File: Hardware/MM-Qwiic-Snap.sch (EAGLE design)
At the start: 37 parts, among them J15 MICROMOD-2222-C, J2 QWIIC_RIGHT_ANGLE, U5 AP7361C-33FGEUDFN-8

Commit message: Preliminary schematic done?
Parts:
- added C3, C4: 4.7uF, SparkFun-Capacitors:4.7UF-0603-35V-(20%)
- added D3: 3A/10V/280mV, SparkFun-DiscreteSemi:DIODE-SCHOTTKY-BAT60A
- added D4: Yellow, SparkFun-LED:LED-YELLOW0603
- added JP1: JUMPER-SMT_2_NC_TRACE_SILK, SparkFun-Jumpers:JUMPER-SMT_2_NC_TRACE_SILK
- added R1: 2.2k, SparkFun-Resistors:2.2KOHM-0603-1/10W-1%
- added R4: 1k, SparkFun-Resistors:1KOHM-0603-1/10W-1%
- added U1: MCP73831, SparkFun-IC-Power:MCP73831
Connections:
- new net 5V: C4.1, D3.C, D4.A, JP1.2, U1.VIN
- new net N$2: R1.2, U1.PROG
- new net N$3: R4.1, U1.STAT
- new net N$5: C3.1, D3.A, J3.+, U1.VBAT
- new net N$8: D4.C, R4.2
- net GND: now also C3.2, C4.2, J3.-, R1.1, U1.VSS
- net VIN: now also JP1.1
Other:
- moved on the sheet: J3

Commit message: Board layout
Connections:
- net 3.3V_EN: now also J15.3.3V_EN
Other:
- note added: "Battery Charger"
- note added: "Buttons"
- note added: "Qwiic Connector"
- note added: "USB-C"
- note removed: "USB"
- moved on the sheet: BYP, C1, C10, C11, C13, C2, C3, C4, C9, D1, D2, D3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

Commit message: Layout
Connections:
- net VIN: now also J15.USB_VIN
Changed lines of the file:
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@@
 <grid distance="0.1" unitdist="inch" unit="inch" style="lines" multiple="1" display="no" altdistance="0.01" altunitdist="inch" altunit="inch"/>
 <layers>
-<layer number="1" name="Top" color="4" fill="1" visible="yes" active="no"/>
-<layer number="2" name="Route2" color="1" fill="3" visible="yes" active="no"/>
-<layer number="3" name="Route3" color="4" fill="3" visible="yes" active="no"/>
-<layer number="4" name="Route4" color="1" fill="4" visible="yes" active="no"/>
-<layer number="5" name="Route5" color="4" fill="4" visible="yes" active="no"/>
-<layer number="6" name="Route6" color="1" fill="8" visible="yes" active="no"/>
-<layer number="7" name="Route7" color="4" fill="8" visible="yes" active="no"/>
-<layer number="8" name="Route8" color="1" fill="2" visible="yes" active="no"/>
-<layer number="9" name="Route9" color="4" fill="2" visible="yes" active="no"/>
-<layer number="10" name="Route10" color="1" fill="7" visible="yes" active="no"/>
-<layer number="11" name="Route11" color="4" fill="7" visible="yes" active="no"/>
-<layer number="12" name="Route12" color="1" fill="5" visible="yes" active="no"/>
-<layer number="13" name="Route13" color="4" fill="5" visible="yes" active="no"/>
-<layer number="14" name="Route14" color="1" fill="6" visible="yes" active="no"/>
-<layer number="15" name="Route15" color="4" fill="6" visible="yes" active="no"/>
-<layer number="16" name="Bottom" color="1" fill="1" visible="yes" active="no"/>
-<layer number="17" name="Pads" color="2" fill="1" visible="yes" active="no"/>
-<layer number="18" name="Vias" color="2" fill="1" visible="yes" active="no"/>
-<layer number="19" name="Unrouted" color="6" fill="1" visible="yes" active="no"/>
-<layer number="20" name="Dimension" color="24" fill="1" visible="yes" active="no"/>
-<layer number="21" name="tPlace" color="16" fill="1" visible="yes" active="no"/>
-<layer number="22" name="bPlace" color="14" fill="1" visible="yes" active="no"/>
-<layer number="23" name="tOrigins" color="15" fill="1" visible="yes" active="no"/>
-<layer number="24" name="bOrigins" color="15" fill="1" visible="yes" active="no"/>
-<layer number="25" name="tNames" color="7" fill="1" visible="yes" active="no"/>
-<layer number="26" name="bNames" color="7" fill="1" visible="yes" active="no"/>
-<layer number="27" name="tValues" color="7" fill="1" visible="yes" active="no"/>
-<layer number="28" name="bValues" color="7" fill="1" visible="yes" active="no"/>
+<layer number="1" name="Top" color="4" fill="1" visible="no" active="no"/>
+<layer number="2" name="Route2" color="1" fill="3" visible="no" active="no"/>
+<layer number="3" name="Route3" color="4" fill="3" visible="no" active="no"/>
+<layer number="4" name="Route4" color="1" fill="4" visible="no" active="no"/>
+<layer number="5" name="Route5" color="4" fill="4" visible="no" active="no"/>
+<layer number="6" name="Route6" color="1" fill="8" visible="no" active="no"/>
+<layer number="7" name="Route7" color="4" fill="8" visible="no" active="no"/>
+<layer number="8" name="Route8" color="1" fill="2" visible="no" active="no"/>
+<layer number="9" name="Route9" color="4" fill="2" visible="no" active="no"/>
+<layer number="10" name="Route10" color="1" fill="7" visible="no" active="no"/>
+<layer number="11" name="Route11" color="4" fill="7" visible="no" active="no"/>
+<layer number="12" name="Route12" color="1" fill="5" visible="no" active="no"/>
+<layer number="13" name="Route13" color="4" fill="5" visible="no" active="no"/>
+<layer number="14" name="Route14" color="1" fill="6" visible="no" active="no"/>
+<layer number="15" name="Route15" color="4" fill="6" visible="no" active="no"/>
+<layer number="16" name="Bottom" color="1" fill="1" visible="no" active="no"/>
+<layer number="17" name="Pads" color="2" fill="1" visible="no" active="no"/>
+<layer number="18" name="Vias" color="2" fill="1" visible="no" active="no"/>
+<layer number="19" name="Unrouted" color="6" fill="1" visible="no" active="no"/>
+<layer number="20" name="Dimension" color="24" fill="1" visible="no" active="no"/>
+<layer number="21" name="tPlace" color="16" fill="1" visible="no" active="no"/>
+<layer number="22" name="bPlace" color="14" fill="1" visible="no" active="no"/>
+<layer number="23" name="tOrigins" color="15" fill="1" visible="no" active="no"/>
+<layer number="24" name="bOrigins" color="15" fill="1" visible="no" active="no"/>
+<layer number="25" name="tNames" color="7" fill="1" visible="no" active="no"/>
+<layer number="26" name="bNames" color="7" fill="1" visible="no" active="no"/>
+<layer number="27" name="tValues" color="7" fill="1" visible="no" active="no"/>
+<layer number="28" name="bValues" color="7" fill="1" visible="no" active="no"/>
 <layer number="29" name="tStop" color="7" fill="3" visible="no" active="no"/>
 <layer number="30" name="bStop" color="7" fill="6" visible="no" active="no"/>
@@
 <layer number="35" name="tGlue" color="7" fill="4" visible="no" active="no"/>
 <layer number="36" name="bGlue" color="7" fill="5" visible="no" active="no"/>
-<layer number="37" name="tTest" color="7" fill="1" visible="yes" active="no"/>
-<layer number="38" name="bTest" color="7" fill="1" visible="yes" active="no"/>
+<layer number="37" name="tTest" color="7" fill="1" visible="no" active="no"/>
+<layer number="38" name="bTest" color="7" fill="1" visible="no" active="no"/>
 <layer number="39" name="tKeepout" color="4" fill="11" visible="no" active="no"/>
 <layer number="40" name="bKeepout" color="1" fill="11" visible="no" active="no"/>
@@
 <layer number="44" name="Drills" color="7" fill="1" visible="no" active="no"/>
 <layer number="45" name="Holes" color="7" fill="1" visible="no" active="no"/>
-<layer number="46" name="Milling" color="3" fill="1" visible="yes" active="no"/>
-<layer number="47" name="Measures" color="7" fill="1" visible="yes" active="no"/>
-<layer number="48" name="Document" color="7" fill="1" visible="yes" active="no"/>
-<layer number="49" name="Reference" color="7" fill="1" visible="yes" active="no"/>
-<layer number="50" name="dxf" color="7" fill="1" visible="yes" active="no"/>
-<layer number="51" name="tDocu" color="6" fill="1" visible="yes" active="no"/>
-<layer number="52" name="bDocu" color="7" fill="1" visible="yes" active="no"/>
-<layer number="53" name="tGND_GNDA" color="7" fill="9" visible="yes" active="no"/>
-<layer number="54" name="bGND_GNDA" color="1" fill="9" visible="yes" active="no"/>
-<layer number="56" name="wert" color="7" fill="1" visible="yes" active="no"/>
-<layer number="57" name="tCAD" color="7" fill="1" visible="yes" active="no"/>
-<layer number="59" name="tCarbon" color="7" fill="1" visible="yes" active="no"/>
-<layer number="60" name="bCarbon" color="7" fill="1" visible="yes" active="no"/>
+<layer number="46" name="Milling" color="3" fill="1" visible="no" active="no"/>
+<layer number="47" name="Measures" color="7" fill="1" visible="no" active="no"/>
+<layer number="48" name="Document" color="7" fill="1" visible="no" active="no"/>
+<layer number="49" name="Reference" color="7" fill="1" visible="no" active="no"/>
+<layer number="50" name="dxf" color="7" fill="1" visible="no" active="no"/>
+<layer number="51" name="tDocu" color="6" fill="1" visible="no" active="no"/>
+<layer number="52" name="bDocu" color="7" fill="1" visible="no" active="no"/>
+<layer number="53" name="tGND_GNDA" color="7" fill="9" visible="no" active="no"/>
+<layer number="54" name="bGND_GNDA" color="1" fill="9" visible="no" active="no"/>
+<layer number="56" name="wert" color="7" fill="1" visible="no" active="no"/>
+<layer number="57" name="tCAD" color="7" fill="1" visible="no" active="no"/>
+<layer number="59" name="tCarbon" color="7" fill="1" visible="no" active="no"/>
+<layer number="60" name="bCarbon" color="7" fill="1" visible="no" active="no"/>
 <layer number="88" name="SimResults" color="9" fill="1" visible="yes" active="yes"/>
 <layer number="89" name="SimProbes" color="9" fill="1" visible="yes" active="yes"/>
@@
 <part name="SUPPLY7" library="SparkFun-PowerSymbols" deviceset="VIN" device=""/>
 <part name="SUPPLY8" library="SparkFun-PowerSymbols" deviceset="VIN" device=""/>
+<part name="SUPPLY9" library="SparkFun-PowerSymbols" deviceset="VIN" device=""/>
 </parts>
 <sheets>
@@
 <attribute name="VALUE" x="261.62" y="251.714" size="1.778" layer="96" align="bottom-center"/>
 </instance>
+<instance part="SUPPLY9" gate="G$1" x="22.86" y="236.22" smashed="yes">
+<attribute name="VALUE" x="22.86" y="239.014" size="1.778" layer="96" align="bottom-center"/>
+</instance>
 </instances>
 <busses>
@@
 <pinref part="SUPPLY4" gate="G$1" pin="VIN"/>
 </segment>
-</net>
+<segment>
+<pinref part="J15" gate="J1" pin="USB_VIN"/>
+<wire x1="38.1" y1="233.68" x2="22.86" y2="233.68" width="0.1524" layer="91"/>
+<wire x1="22.86" y1="233.68" x2="22.86" y2="236.22" width="0.1524" layer="91"/>
+<pinref part="SUPPLY9" gate="G$1" pin="VIN"/>
+</segment>
+</net>

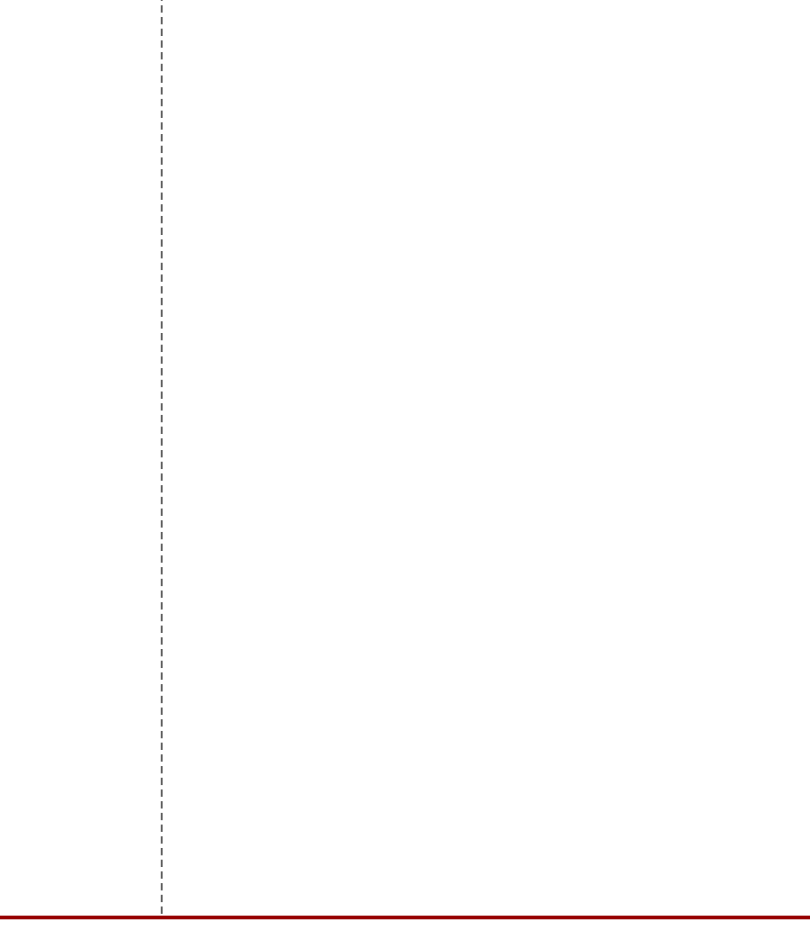
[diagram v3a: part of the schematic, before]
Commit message: Created part for stand off, proto layout finished
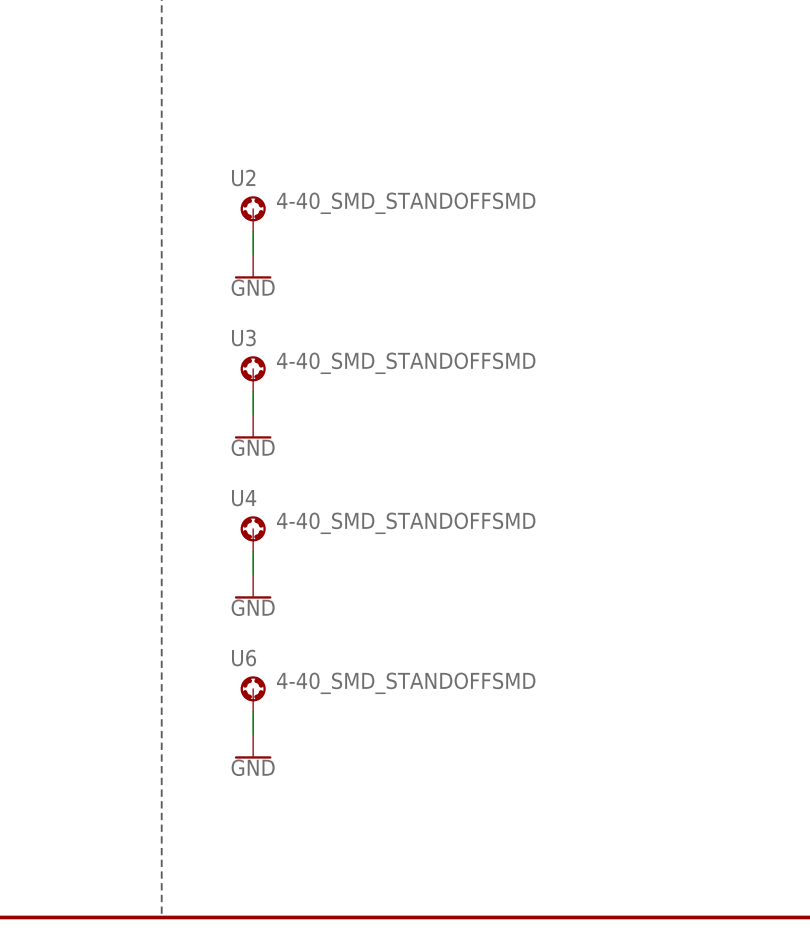
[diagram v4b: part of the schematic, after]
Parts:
- added U2, U3, U4, U6: 4-40_SMD_STANDOFFSMD, qwiic_carrier:4-40_SMD_STANDOFFSMD
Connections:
- net GND: now also U2.1, U3.1, U4.1, U6.1
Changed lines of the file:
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@@
 <part name="SUPPLY8" library="SparkFun-PowerSymbols" deviceset="VIN" device=""/>
 <part name="SUPPLY9" library="SparkFun-PowerSymbols" deviceset="VIN" device=""/>
+<part name="U2" library="qwiic_carrier" deviceset="4-40_SMD_STANDOFF" device="SMD"/>
+<part name="U3" library="qwiic_carrier" deviceset="4-40_SMD_STANDOFF" device="SMD"/>
+<part name="U4" library="qwiic_carrier" deviceset="4-40_SMD_STANDOFF" device="SMD"/>
+<part name="U6" library="qwiic_carrier" deviceset="4-40_SMD_STANDOFF" device="SMD"/>
+<part name="GND7" library="SparkFun-PowerSymbols" deviceset="GND" device=""/>
+<part name="GND11" library="SparkFun-PowerSymbols" deviceset="GND" device=""/>
+<part name="GND12" library="SparkFun-PowerSymbols" deviceset="GND" device=""/>
+<part name="GND13" library="SparkFun-PowerSymbols" deviceset="GND" device=""/>
 </parts>
 <sheets>
@@
 <attribute name="VALUE" x="22.86" y="239.014" size="1.778" layer="96" align="bottom-center"/>
 </instance>
+<instance part="U2" gate="U1" x="261.62" y="78.74" smashed="yes">
+<attribute name="NAME" x="259.08" y="81.28" size="1.778" layer="95"/>
+<attribute name="VALUE" x="264.16" y="78.74" size="1.778" layer="96"/>
+</instance>
+<instance part="U3" gate="U1" x="261.62" y="60.96" smashed="yes">
+<attribute name="NAME" x="259.08" y="63.5" size="1.778" layer="95"/>
+<attribute name="VALUE" x="264.16" y="60.96" size="1.778" layer="96"/>
+</instance>
+<instance part="U4" gate="U1" x="261.62" y="43.18" smashed="yes">
+<attribute name="NAME" x="259.08" y="45.72" size="1.778" layer="95"/>
+<attribute name="VALUE" x="264.16" y="43.18" size="1.778" layer="96"/>
+</instance>
+<instance part="U6" gate="U1" x="261.62" y="25.4" smashed="yes">
+<attribute name="NAME" x="259.08" y="27.94" size="1.778" layer="95"/>
+<attribute name="VALUE" x="264.16" y="25.4" size="1.778" layer="96"/>
+</instance>
+<instance part="GND7" gate="1" x="261.62" y="71.12" smashed="yes">
+<attribute name="VALUE" x="261.62" y="70.866" size="1.778" layer="96" align="top-center"/>
+</instance>
+<instance part="GND11" gate="1" x="261.62" y="53.34" smashed="yes">
+<attribute name="VALUE" x="261.62" y="53.086" size="1.778" layer="96" align="top-center"/>
+</instance>
+<instance part="GND12" gate="1" x="261.62" y="35.56" smashed="yes">
+<attribute name="VALUE" x="261.62" y="35.306" size="1.778" layer="96" align="top-center"/>
+</instance>
+<instance part="GND13" gate="1" x="261.62" y="17.78" smashed="yes">
+<attribute name="VALUE" x="261.62" y="17.526" size="1.778" layer="96" align="top-center"/>
+</instance>
 </instances>
 <busses>
@@
 <pinref part="GND4" gate="1" pin="GND"/>
 </segment>
+<segment>
+<pinref part="U2" gate="U1" pin="1"/>
+<pinref part="GND7" gate="1" pin="GND"/>
+<wire x1="261.62" y1="73.66" x2="261.62" y2="76.2" width="0.1524" layer="91"/>
+</segment>
+<segment>
+<pinref part="U3" gate="U1" pin="1"/>
+<pinref part="GND11" gate="1" pin="GND"/>
+<wire x1="261.62" y1="55.88" x2="261.62" y2="58.42" width="0.1524" layer="91"/>
+</segment>
+<segment>
+<pinref part="U4" gate="U1" pin="1"/>
+<pinref part="GND12" gate="1" pin="GND"/>
+<wire x1="261.62" y1="38.1" x2="261.62" y2="40.64" width="0.1524" layer="91"/>
+</segment>
+<segment>
+<pinref part="U6" gate="U1" pin="1"/>
+<pinref part="GND13" gate="1" pin="GND"/>
+<wire x1="261.62" y1="20.32" x2="261.62" y2="22.86" width="0.1524" layer="91"/>
+</segment>
 </net>
